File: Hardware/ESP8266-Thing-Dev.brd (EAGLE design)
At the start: 55.4 x 25.9 mm, 69 parts, among them J1 DNP, Q1 MMBT2222A, Q2 MMBT2222A, U1 AP2112K-3.3V, U2 ESP8266, U3 AT25SF041-SOIC8, U4 FTS31XS-U, Y1 26MHz

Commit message: Import project and add level shifters in schematic.
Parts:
- added Q4, Q5, Q6, Q7, Q8: BSS138, SparkFun:SOT23-3
- added R20, R21, R22, R23, R24, R25, R26, R27, R28, R29: 10K, SparkFun:0603-RES
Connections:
- new net GPIO0_OUT: JP3.4, Q5.3, R23.2
- new net GPIO12_OUT: JP3.7, Q8.3, R29.2
- new net GPIO13_OUT: JP3.6, Q7.3, R27.2
- new net GPIO4_OUT: JP3.5, Q6.3, R25.2
- new net GPIO5_OUT: JP3.3, Q4.3, R21.2
- new net HV: R21.1, R23.1, R25.1, R27.1, R29.1
- new net LV: Q5.1, Q6.1, Q7.1, Q8.1, R22.1, R24.1, R26.1, R28.1
- net GPIO0: now also Q5.2, R22.2; no longer JP3.4
- net GPIO12: now also Q8.2, R28.2; no longer JP3.7
- net GPIO13: now also Q7.2, R26.2; no longer JP3.6
- net GPIO4: now also Q6.2, R24.2; no longer JP3.5
- net GPIO5: now also Q4.2, R20.2; no longer JP3.3
- net VCC: now also Q4.1, R20.1
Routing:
- net GPIO5: track 21.0 -> 17.2 mm
- net GPIO4: track 10.3 -> 7.56 mm
- net GPIO12: track 9.32 -> 7.45 mm
- net GPIO13: track 10.7 -> 8.95 mm
- net GPIO0: track 29.5 -> 28.2 mm

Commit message: Fix Net names for level shifter supply voltages
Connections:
- removed net HV: R21.1, R23.1, R25.1, R27.1, R29.1
- removed net LV: Q5.1, Q6.1, Q7.1, Q8.1, R22.1, R24.1, R26.1, R28.1
- net VCC: now also Q5.1, Q6.1, Q7.1, Q8.1, R22.1, R24.1, R26.1, R28.1
- net VIN: now also R21.1, R23.1, R25.1, R27.1, R29.1
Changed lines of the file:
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@@
 <contactref element="R20" pad="1"/>
 <contactref element="Q4" pad="1"/>
-<wire x1="-25.334" y1="-26.146" x2="-22.186" y2="-28.194" width="0" layer="19" extent="1-1"/>
-<wire x1="19.05" y1="1.27" x2="-22.186" y2="-28.194" width="0" layer="19" extent="1-1"/>
+<contactref element="R22" pad="1"/>
+<contactref element="Q5" pad="1"/>
+<contactref element="R24" pad="1"/>
+<contactref element="Q6" pad="1"/>
+<contactref element="R26" pad="1"/>
+<contactref element="Q7" pad="1"/>
+<contactref element="R28" pad="1"/>
+<contactref element="Q8" pad="1"/>
+<wire x1="-22.186" y1="-32.258" x2="-22.186" y2="-35.306" width="0" layer="19" extent="1-1"/>
+<wire x1="-25.334" y1="-30.21" x2="-22.186" y2="-32.258" width="0" layer="19" extent="1-1"/>
+<wire x1="-22.186" y1="-28.194" x2="-25.334" y2="-30.21" width="0" layer="19" extent="1-1"/>
+<wire x1="-22.286" y1="-26.146" x2="-22.186" y2="-28.194" width="0" layer="19" extent="1-1"/>
+<wire x1="-25.334" y1="-26.146" x2="-22.286" y2="-26.146" width="0" layer="19" extent="1-1"/>
+<wire x1="-19.238" y1="-26.146" x2="-22.286" y2="-26.146" width="0" layer="19" extent="1-1"/>
+<wire x1="-16.19" y1="-26.146" x2="-19.238" y2="-26.146" width="0" layer="19" extent="1-1"/>
+<wire x1="-16.09" y1="-28.194" x2="-16.19" y2="-26.146" width="0" layer="19" extent="1-1"/>
+<wire x1="-16.09" y1="-32.258" x2="-16.09" y2="-28.194" width="0" layer="19" extent="1-1"/>
+<wire x1="19.05" y1="1.27" x2="-16.19" y2="-26.146" width="0" layer="19" extent="1-1"/>
 </signal>
 <signal name="GND">
@@
 <wire x1="8.375" y1="12.954" x2="7.62" y2="12.954" width="0.4064" layer="1"/>
 <wire x1="7.62" y1="12.954" x2="7.366" y2="13.208" width="0.4064" layer="1"/>
+<contactref element="R21" pad="1"/>
+<contactref element="R23" pad="1"/>
+<contactref element="R25" pad="1"/>
+<contactref element="R27" pad="1"/>
+<contactref element="R29" pad="1"/>
+<wire x1="-25.234" y1="-32.258" x2="-25.234" y2="-35.306" width="0" layer="19" extent="1-1"/>
+<wire x1="-19.138" y1="-35.306" x2="-25.234" y2="-35.306" width="0" layer="19" extent="1-1"/>
+<wire x1="-19.138" y1="-32.258" x2="-19.138" y2="-35.306" width="0" layer="19" extent="1-1"/>
+<wire x1="-19.138" y1="-28.194" x2="-19.138" y2="-32.258" width="0" layer="19" extent="1-1"/>
+<wire x1="7.62" y1="12.954" x2="-19.138" y2="-28.194" width="0" layer="19" extent="1-1"/>
 </signal>
 <signal name="RTS">
@@
 <wire x1="45.847" y1="11.811" x2="46.017178125" y2="13.081" width="0.762" layer="1" curve="22.585118"/>
 </signal>
-<signal name="LV">
-<contactref element="R22" pad="1"/>
-<contactref element="Q5" pad="1"/>
-<contactref element="R24" pad="1"/>
-<contactref element="Q6" pad="1"/>
-<contactref element="R26" pad="1"/>
-<contactref element="Q7" pad="1"/>
-<contactref element="R28" pad="1"/>
-<contactref element="Q8" pad="1"/>
-<wire x1="-22.186" y1="-32.258" x2="-22.186" y2="-35.306" width="0" layer="19" extent="1-1"/>
-<wire x1="-25.334" y1="-30.21" x2="-22.186" y2="-32.258" width="0" layer="19" extent="1-1"/>
-<wire x1="-22.286" y1="-26.146" x2="-25.334" y2="-30.21" width="0" layer="19" extent="1-1"/>
-<wire x1="-19.238" y1="-26.146" x2="-22.286" y2="-26.146" width="0" layer="19" extent="1-1"/>
-<wire x1="-16.19" y1="-26.146" x2="-19.238" y2="-26.146" width="0" layer="19" extent="1-1"/>
-<wire x1="-16.09" y1="-28.194" x2="-16.19" y2="-26.146" width="0" layer="19" extent="1-1"/>
-<wire x1="-16.09" y1="-32.258" x2="-16.09" y2="-28.194" width="0" layer="19" extent="1-1"/>
-</signal>
 <signal name="GPIO5_OUT">
 <contactref element="Q4" pad="3"/>
@@
 <wire x1="21.59" y1="24.13" x2="-17.438" y2="-28.194" width="0" layer="19" extent="1-1"/>
 </signal>
-<signal name="HV">
-<contactref element="R21" pad="1"/>
-<contactref element="R23" pad="1"/>
-<contactref element="R25" pad="1"/>
-<contactref element="R27" pad="1"/>
-<contactref element="R29" pad="1"/>
-<wire x1="-25.234" y1="-32.258" x2="-25.234" y2="-35.306" width="0" layer="19" extent="1-1"/>
-<wire x1="-19.138" y1="-35.306" x2="-25.234" y2="-35.306" width="0" layer="19" extent="1-1"/>
-<wire x1="-19.138" y1="-32.258" x2="-19.138" y2="-35.306" width="0" layer="19" extent="1-1"/>
-<wire x1="-19.138" y1="-28.194" x2="-19.138" y2="-32.258" width="0" layer="19" extent="1-1"/>
-</signal>
 <signal name="GPIO13_OUT">

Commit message: Move level shift transistors above appropriate parts. Just a stopping point for the night.
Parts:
- moved R27 90.0 mm to (29.5, 36.8)
- moved R29 88.5 mm to (33.0, 36.8)
- moved R28 85.3 mm to (33.0, 30.5)
- moved Q8 84.8 mm to (33.0, 33.3)
- moved R23 83.4 mm to (22.4, 36.8)
- moved R25 82.0 mm to (25.9, 36.8)
- moved R24 78.8 mm to (26.4, 30.5)
- moved R26 77.2 mm to (29.7, 30.5)
- moved R21 74.9 mm to (18.8, 36.8)
- moved Q7 73.7 mm to (29.7, 33.3)
- moved Q6 73.6 mm to (26.4, 33.3)
- moved Q5 73.4 mm to (23.1, 33.3)
- moved Q4 73.3 mm to (19.8, 33.3)
- moved R20 71.7 mm to (19.8, 30.5)
- moved R22 70.1 mm to (23.1, 30.5)

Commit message: Move level shifter on GPIO 0 to GPIO 15.
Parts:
- moved Q5 16.0 mm to (39.1, 33.3)
- moved R22 16.0 mm to (39.1, 30.5)
- moved R23 16.0 mm to (38.4, 36.8)
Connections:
- removed net GPIO0_OUT: JP3.4, Q5.3, R23.2
- new net GPIO15_OUT: JP3.10, Q5.3, R23.2
- net GPIO0: now also JP3.4; no longer Q5.2, R22.2
- net GPIO15: now also Q5.2, R22.2; no longer JP3.10
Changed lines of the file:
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@@
 <element name="R20" library="SparkFun" package="0603-RES" value="10K" x="19.812" y="30.48"/>
 <element name="R21" library="SparkFun" package="0603-RES" value="10K" x="18.796" y="36.83"/>
-<element name="Q5" library="SparkFun" package="SOT23-3" value="BSS138" x="23.114" y="33.274"/>
-<element name="R22" library="SparkFun" package="0603-RES" value="10K" x="23.114" y="30.48"/>
-<element name="R23" library="SparkFun" package="0603-RES" value="10K" x="22.352" y="36.83"/>
+<element name="Q5" library="SparkFun" package="SOT23-3" value="BSS138" x="39.116" y="33.274"/>
+<element name="R22" library="SparkFun" package="0603-RES" value="10K" x="39.116" y="30.48"/>
+<element name="R23" library="SparkFun" package="0603-RES" value="10K" x="38.354" y="36.83"/>
 <element name="Q6" library="SparkFun" package="SOT23-3" value="BSS138" x="26.416" y="33.274"/>
 <element name="R24" library="SparkFun" package="0603-RES" value="10K" x="26.416" y="30.48"/>
@@
 <wire x1="32.07" y1="32.274" x2="25.566" y2="30.48" width="0" layer="19" extent="1-1"/>
 <wire x1="18.962" y1="30.48" x2="32.07" y2="32.274" width="0" layer="19" extent="1-1"/>
-<wire x1="22.164" y1="32.274" x2="18.962" y2="30.48" width="0" layer="19" extent="1-1"/>
-<wire x1="18.862" y1="32.274" x2="22.164" y2="32.274" width="0" layer="19" extent="1-1"/>
-<wire x1="25.466" y1="32.274" x2="22.164" y2="32.274" width="0" layer="19" extent="1-1"/>
+<wire x1="38.166" y1="32.274" x2="18.962" y2="30.48" width="0" layer="19" extent="1-1"/>
+<wire x1="18.862" y1="32.274" x2="38.166" y2="32.274" width="0" layer="19" extent="1-1"/>
+<wire x1="25.466" y1="32.274" x2="38.166" y2="32.274" width="0" layer="19" extent="1-1"/>
 <wire x1="28.768" y1="32.274" x2="25.466" y2="32.274" width="0" layer="19" extent="1-1"/>
-<wire x1="22.264" y1="30.48" x2="28.768" y2="32.274" width="0" layer="19" extent="1-1"/>
-<wire x1="28.868" y1="30.48" x2="22.264" y2="30.48" width="0" layer="19" extent="1-1"/>
+<wire x1="38.266" y1="30.48" x2="28.768" y2="32.274" width="0" layer="19" extent="1-1"/>
+<wire x1="28.868" y1="30.48" x2="38.266" y2="30.48" width="0" layer="19" extent="1-1"/>
 <wire x1="19.05" y1="1.27" x2="28.768" y2="32.274" width="0" layer="19" extent="1-1"/>
 </signal>
@@
 <wire x1="30.48" y1="22.098" x2="24.13" y2="22.098" width="0.2032" layer="16"/>
 <wire x1="24.13" y1="22.098" x2="24.13" y2="22.86" width="0.2032" layer="16"/>
-<contactref element="Q5" pad="2"/>
-<contactref element="R22" pad="2"/>
-<wire x1="23.964" y1="30.48" x2="24.064" y2="32.274" width="0" layer="19" extent="1-1"/>
-<wire x1="25.4" y1="11.895" x2="23.964" y2="30.48" width="0" layer="19" extent="1-1"/>
+<contactref element="JP3" pad="4"/>
+<wire x1="24.13" y1="22.86" x2="24.13" y2="24.13" width="0" layer="19" extent="16-16"/>
 </signal>
 <signal name="GPIO5">
@@
 <contactref element="U2" pad="13"/>
 <contactref element="R17" pad="2"/>
-<contactref element="JP3" pad="10"/>
 <via x="34.29" y="20.7518" extent="1-16" drill="0.381"/>
 <via x="36.703" y="22.352" extent="1-16" drill="0.381"/>
 <wire x1="39.282" y1="21.258" x2="39.282" y2="22.352" width="0.2032" layer="1"/>
 <wire x1="39.282" y1="22.352" x2="39.282" y2="24.042" width="0.2032" layer="1"/>
-<wire x1="39.282" y1="24.042" x2="39.37" y2="24.13" width="0.2032" layer="1"/>
 <wire x1="34.04" y1="17.74" x2="34.04" y2="20.5018" width="0.2032" layer="1"/>
 <wire x1="34.04" y1="20.5018" x2="34.29" y2="20.7518" width="0.2032" layer="1"/>
@@
 <wire x1="35.8902" y1="22.352" x2="36.703" y2="22.352" width="0.2032" layer="16"/>
 <wire x1="36.703" y1="22.352" x2="39.282" y2="22.352" width="0.2032" layer="1"/>
+<contactref element="Q5" pad="2"/>
+<contactref element="R22" pad="2"/>
+<wire x1="39.966" y1="30.48" x2="40.066" y2="32.274" width="0" layer="19" extent="1-1"/>
+<wire x1="34.04" y1="20.5018" x2="39.966" y2="30.48" width="0" layer="19" extent="1-1"/>
 </signal>
 <signal name="GPIO13">
@@
 <contactref element="R27" pad="1"/>
 <contactref element="R29" pad="1"/>
-<wire x1="21.502" y1="36.83" x2="28.614" y2="36.83" width="0" layer="19" extent="1-1"/>
+<wire x1="37.504" y1="36.83" x2="28.614" y2="36.83" width="0" layer="19" extent="1-1"/>
 <wire x1="32.17" y1="36.83" x2="28.614" y2="36.83" width="0" layer="19" extent="1-1"/>
 <wire x1="25.058" y1="36.83" x2="32.17" y2="36.83" width="0" layer="19" extent="1-1"/>
@@
 <wire x1="26.758" y1="36.83" x2="26.416" y2="34.374" width="0" layer="19" extent="1-1"/>
 </signal>
-<signal name="GPIO0_OUT">
+<signal name="GPIO15_OUT">
+<contactref element="JP3" pad="10"/>
 <contactref element="Q5" pad="3"/>
 <contactref element="R23" pad="2"/>
-<contactref element="JP3" pad="4"/>
-<wire x1="23.114" y1="34.374" x2="23.202" y2="36.83" width="0" layer="19" extent="1-1"/>
-<wire x1="24.13" y1="24.13" x2="23.114" y2="34.374" width="0" layer="19" extent="1-1"/>
+<wire x1="39.116" y1="34.374" x2="39.37" y2="24.13" width="0" layer="19" extent="1-1"/>
+<wire x1="39.204" y1="36.83" x2="39.116" y2="34.374" width="0" layer="19" extent="1-1"/>
 </signal>
 </signals>

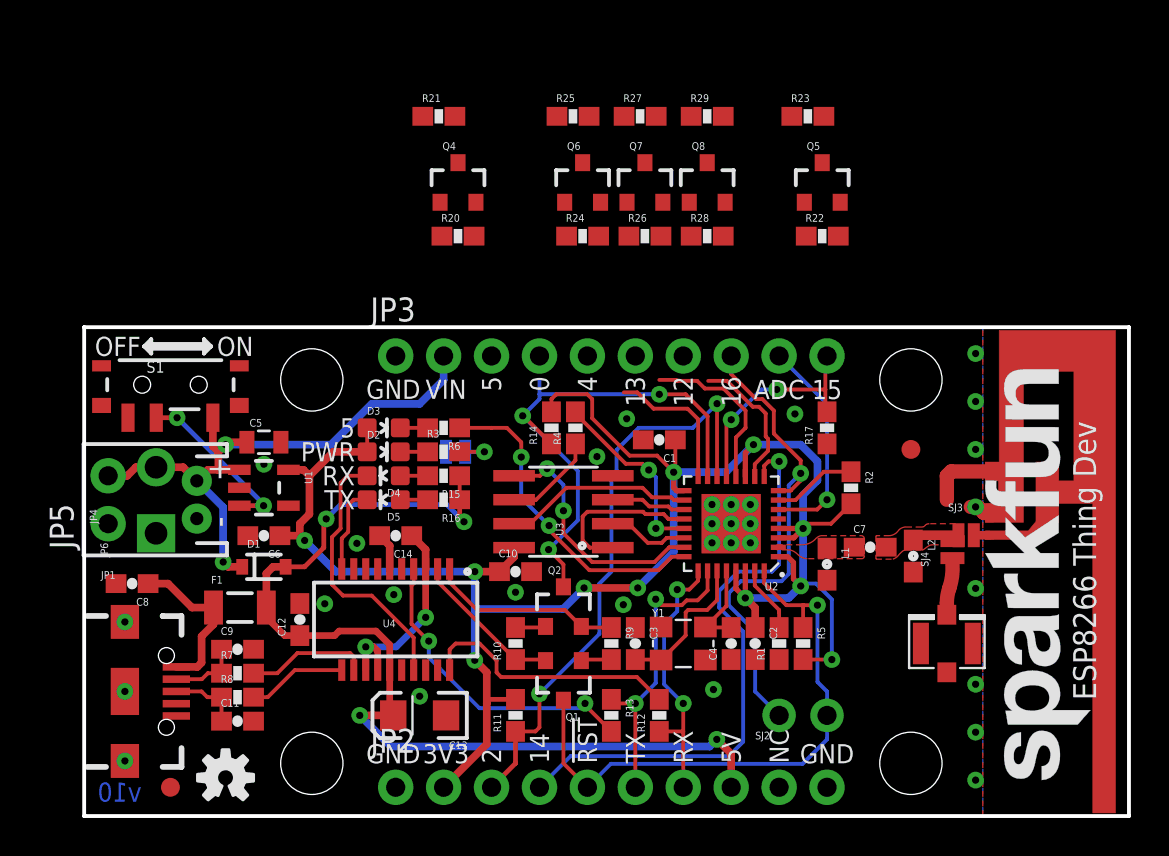
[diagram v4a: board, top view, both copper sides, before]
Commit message: Switch to 7 pin header. Make board outline larger.
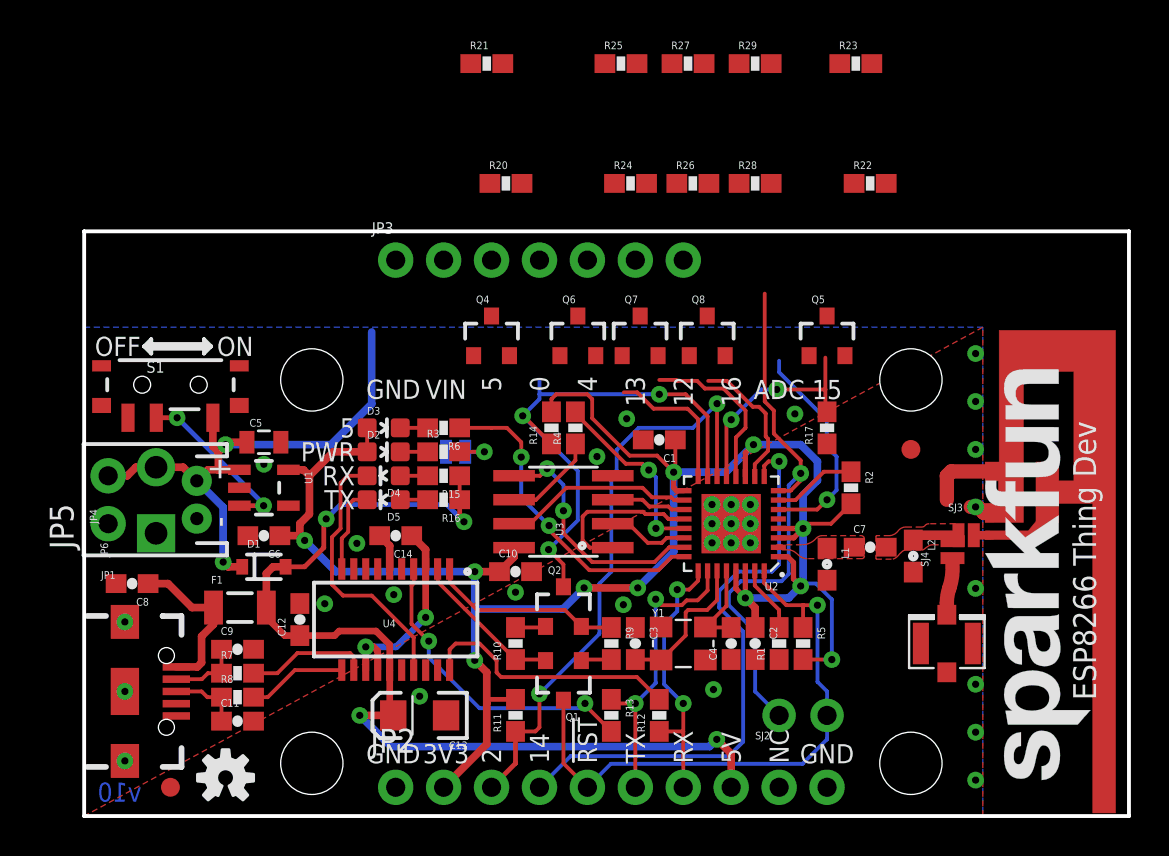
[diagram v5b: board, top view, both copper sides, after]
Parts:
- JP3: device SparkFun-Connectors:1X10_NO_SILK -> SparkFun-Connectors:1X07_NO_SILK
- moved Q4 8.32 mm to (21.6, 25.1)
- moved Q5 8.13 mm to (39.4, 25.1)
- moved Q6 8.13 mm to (26.2, 25.1)
- moved Q7 8.13 mm to (29.5, 25.1)
- moved Q8 8.13 mm to (33.0, 25.1)
- moved JP3 5.08 mm to (16.5, 29.2)
- moved R21 3.78 mm to (21.3, 39.6)
- moved R23 3.78 mm to (40.9, 39.6)
- moved R25 3.78 mm to (28.4, 39.6)
- moved R27 3.78 mm to (32.0, 39.6)
- moved R29 3.78 mm to (35.6, 39.6)
- moved R26 3.78 mm to (32.3, 33.3)
- moved R20 3.78 mm to (22.4, 33.3)
- moved R22 3.78 mm to (41.7, 33.3)
- moved R24 3.78 mm to (29.0, 33.3)
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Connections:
- net ADC: no longer JP3.9
- net GPIO0: no longer JP3.4
- net GPIO12_OUT: now also JP3.6; no longer JP3.7
- net GPIO13_OUT: now also JP3.5; no longer JP3.6
- net GPIO15_OUT: now also JP3.7; no longer JP3.10
- net GPIO16: no longer JP3.8
- net GPIO4_OUT: now also JP3.4; no longer JP3.5
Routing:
- net GPIO16: track 26.5 -> 28.9 mm
- net VIN: track 32.5 -> 30.7 mm
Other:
- board size 55.4 x 25.9 mm -> 55.4 x 31 mm

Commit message: Position level shifter components.
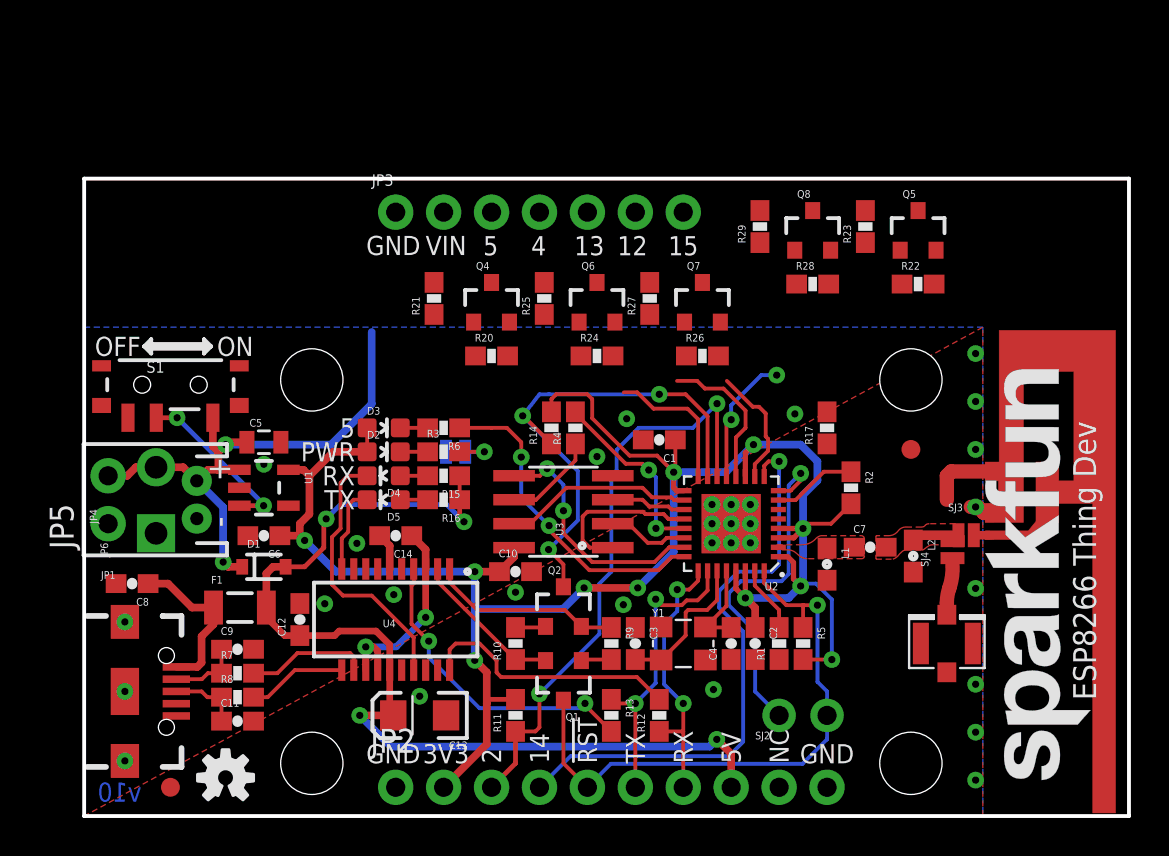
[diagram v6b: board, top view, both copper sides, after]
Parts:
- moved R25 13.1 mm to (24.4, 27.2), turned to 90 degrees
- moved R21 12.8 mm to (18.5, 27.2), turned to 90 degrees
- moved R27 12.6 mm to (30.0, 27.2), turned to 90 degrees
- moved R24 9.32 mm to (27.2, 24.1)
- moved R20 9.18 mm to (21.6, 24.1)
- moved R26 9.16 mm to (32.8, 24.1)
- moved R23 8.65 mm to (41.4, 31.0), turned to 90 degrees
- moved R29 8.64 mm to (35.8, 31.0), turned to 90 degrees
- moved Q8 7.90 mm to (38.6, 30.7)
- moved Q5 7.38 mm to (44.2, 30.7)
- moved R28 6.14 mm to (38.6, 27.9)
- moved R22 5.91 mm to (44.2, 27.9)
- moved Q7 3.75 mm to (32.8, 26.9)
- moved JP3 2.54 mm to (16.5, 31.8)
- moved Q6 2.05 mm to (27.2, 26.9)
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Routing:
- net ADC: track 11.6 -> 0.00 mm, vias 1 -> 0
- net GPIO16: track 28.9 -> 18.6 mm
- net GPIO15: track 11.7 -> 7.08 mm
- net GPIO12: track 7.45 -> 6.46 mm
- net GPIO13: track 8.95 -> 7.99 mm
- net GPIO0: track 28.2 -> 27.4 mm
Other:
- board size 55.4 x 31 mm -> 55.4 x 33.8 mm
- board text removed: "0"
- board text removed: "16"
- board text removed: "ADC"
